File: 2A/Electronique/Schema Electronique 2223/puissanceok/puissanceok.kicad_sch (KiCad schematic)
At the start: 30 parts, among them J101 Bat 2, J102 Bat 1, J103 AU, J104 Switch, J11 Conn_01x05, J113 Conn_02x20_Odd_Even, J18 Conn_01x02, J19 Conn_01x02, J20 Conn_01x02, J21 Conn_01x02, J7 Conn_01x02, J9 Conn_01x05

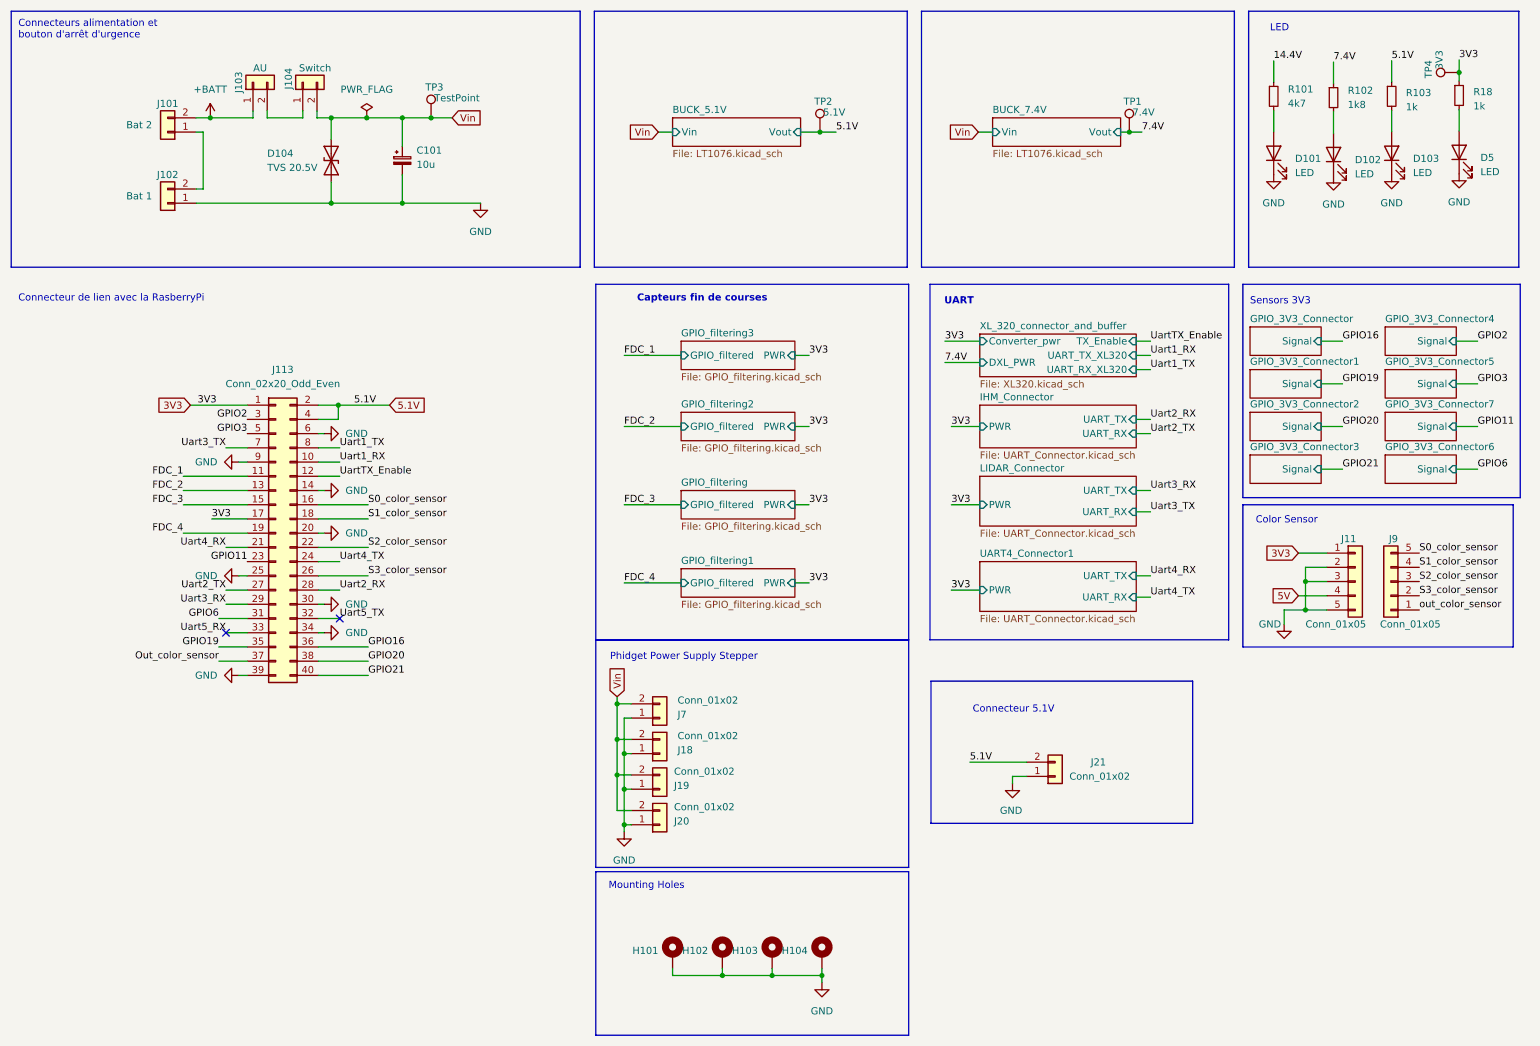
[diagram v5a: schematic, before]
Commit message: update schematic
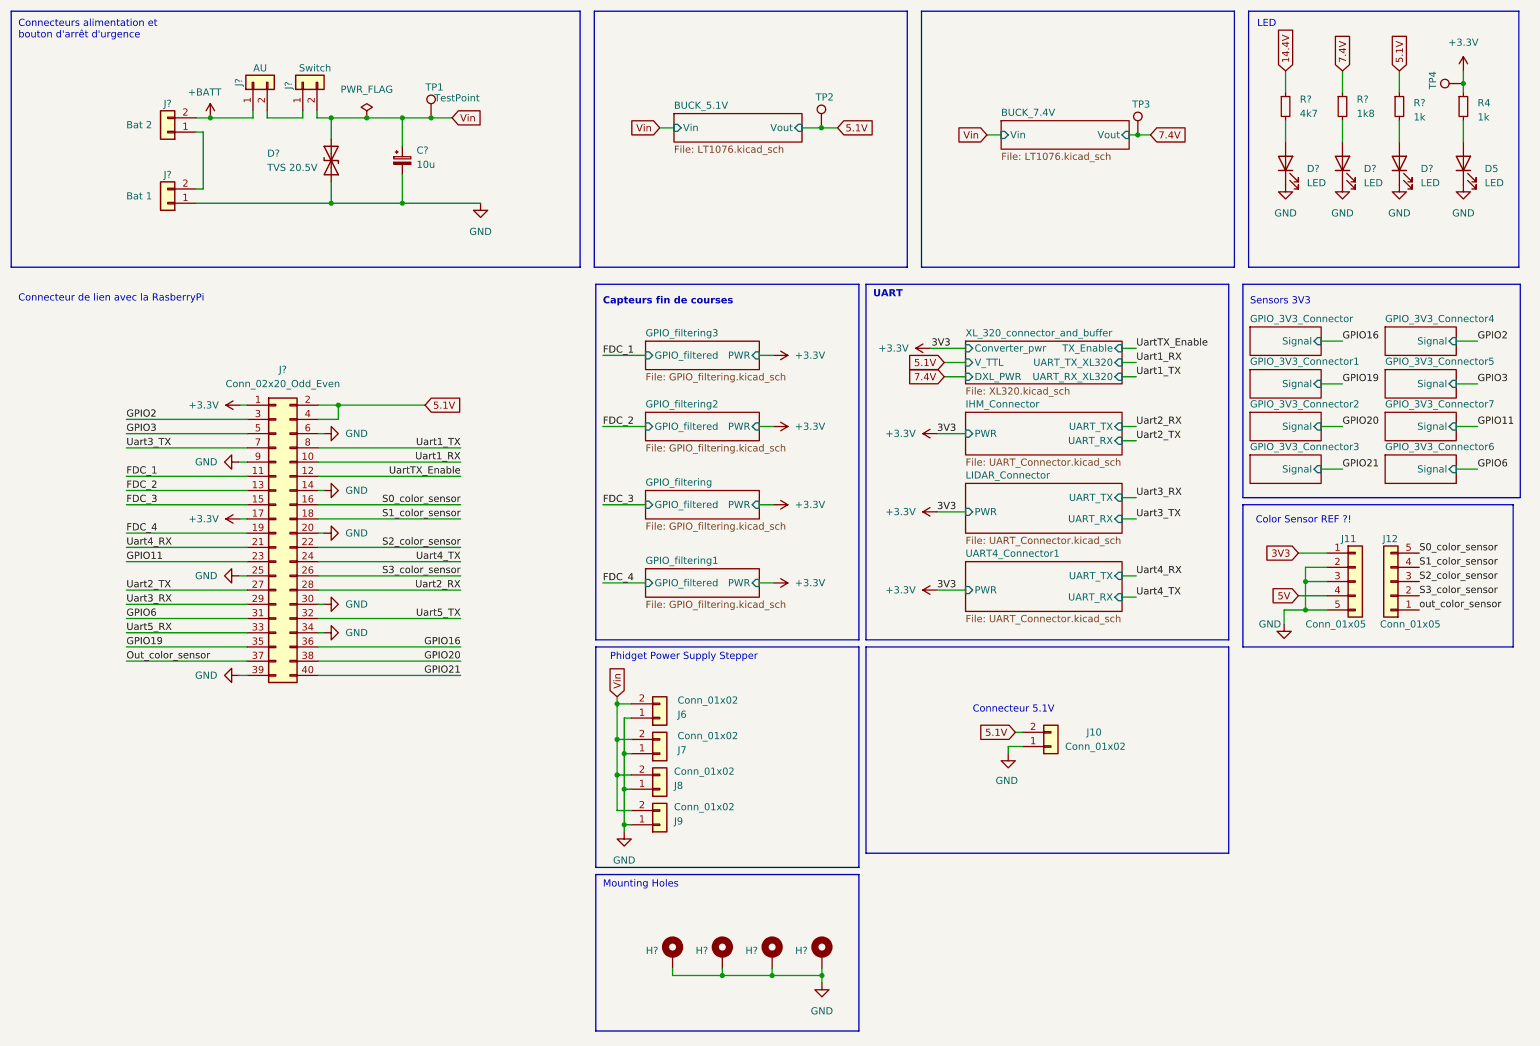
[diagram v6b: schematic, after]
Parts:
- renumbered C101 to C?, D101 to D?, D102 to D?, D104 to D?, D103 to D?, H102 to H?, H101 to H?, H103 to H?, H104 to H?, J21 to J10, J9 to J12, J7 to J6, J18 to J7, J19 to J8, J20 to J9, J102 to J?, J103 to J?, J113 to J?, J104 to J?, J101 to J?, R18 to R4, R101 to R?, R102 to R?, R103 to R?, TP3 to TP1, TP1 to TP3
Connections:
- net 3V3 renamed +3.3V
- no-connect marks 2 -> 0
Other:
- sheet XL_320_connector_and_buffer ports: added V_TTL; removed none
- note added: "Color Sensor REF ?!"
- note removed: "Color Sensor"
- moved on the sheet: D5, D?, J10, R4, R?, TP2, TP3, TP4

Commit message: debut assignation empreintes
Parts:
- C?: footprint Capacitor_SMD:CP_Elec_5x5.4 -> Capacitor_SMD:C_0603_1608Metric_Pad1.08x0.95mm_HandSolder
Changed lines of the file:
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@@
       (effects (font (size 1.27 1.27)) (justify left))
     )
-    (property "Footprint" "Capacitor_SMD:CP_Elec_5x5.4" (at 83.566 41.402 0)
+    (property "Footprint" "Capacitor_SMD:C_0603_1608Metric_Pad1.08x0.95mm_HandSolder" (at 83.566 41.402 0)
       (effects (font (size 1.27 1.27)) hide)
     )

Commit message: update pcd
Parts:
- added J5, J6, J7: Conn_01x08, Connector_PinHeader_2.54mm:PinHeader_1x08_P2.54mm_Vertical, symbol Connector_Generic:Conn_01x08
- C?: footprint Capacitor_SMD:C_0603_1608Metric_Pad1.08x0.95mm_HandSolder -> (none)
- D5, D? (x3): footprint LED_SMD:LED_0603_1608Metric_Pad1.05x0.95mm_HandSolder -> LED_SMD:LED_0603_1608Metric
- J10: renamed from J12; footprint (none) -> Connector_JST:JST_XH_B5B-XH-A_1x05_P2.50mm_Vertical
- J11: renamed from J6; footprint (none) -> Connector_JST:JST_XH_B2B-XH-A_1x02_P2.50mm_Vertical
- J12: renamed from J10; footprint (none) -> Connector_JST:JST_XH_B2B-XH-A_1x02_P2.50mm_Vertical
- J13: renamed from J7; footprint (none) -> Connector_JST:JST_XH_B2B-XH-A_1x02_P2.50mm_Vertical
- J14: renamed from J8; footprint (none) -> Connector_JST:JST_XH_B2B-XH-A_1x02_P2.50mm_Vertical
- J15: renamed from J9; footprint (none) -> Connector_JST:JST_XH_B2B-XH-A_1x02_P2.50mm_Vertical
- J9: renamed from J11; footprint (none) -> Connector_JST:JST_XH_B5B-XH-A_1x05_P2.50mm_Vertical
- J?: footprint (none) -> Connector_PinSocket_2.54mm:PinSocket_2x20_P2.54mm_Vertical
- TP1: renamed from TP4; footprint (none) -> Connector_Pin:Pin_D0.9mm_L10.0mm_W2.4mm_FlatFork
- TP2: renamed from TP1; footprint (none) -> Connector_Pin:Pin_D0.9mm_L10.0mm_W2.4mm_FlatFork
- TP3: renamed from TP2; footprint (none) -> Connector_Pin:Pin_D0.9mm_L10.0mm_W2.4mm_FlatFork
- TP4: renamed from TP3; footprint (none) -> Connector_Pin:Pin_D0.9mm_L10.0mm_W2.4mm_FlatFork
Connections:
- net +3.3V: now also J7.1 (Pin_1), J7.2 (Pin_2), J7.3 (Pin_3), J7.4 (Pin_4), J7.5 (Pin_5), J7.6 (Pin_6), J7.7 (Pin_7), J7.8 (Pin_8); no longer J9.1 (Pin_1)
- net GND: now also J5.1 (Pin_1), J5.2 (Pin_2), J5.3 (Pin_3), J5.4 (Pin_4), J5.5 (Pin_5), J5.6 (Pin_6), J5.7 (Pin_7), J5.8 (Pin_8)
- net GPIO11: now also J6.4 (Pin_4)
- net GPIO16: now also J6.5 (Pin_5)
- net GPIO19: now also J6.6 (Pin_6)
- net GPIO2: now also J6.1 (Pin_1)
- net GPIO20: now also J6.7 (Pin_7)
- net GPIO21: now also J6.8 (Pin_8)
- net GPIO3: now also J6.2 (Pin_2)
- net GPIO6: now also J6.3 (Pin_3)
- new net 3V3: J9.1 (Pin_1)
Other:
- removed sheet GPIO_3V3_Connector
- removed sheet GPIO_3V3_Connector1
- removed sheet GPIO_3V3_Connector2
- removed sheet GPIO_3V3_Connector3
- removed sheet GPIO_3V3_Connector4
- removed sheet GPIO_3V3_Connector5
- removed sheet GPIO_3V3_Connector6
- removed sheet GPIO_3V3_Connector7
- note added: "Color Sensor TCS230"
- note added: "GPIO unused"
- note removed: "Color Sensor REF ?!"
- note removed: "Sensors 3V3"
- moved on the sheet: J?, TP1, TP3, TP4
